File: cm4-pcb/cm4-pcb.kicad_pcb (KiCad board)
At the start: 2 copper layers, 140 x 70.5 mm, 40 parts, among them J1 Conn_01x02_Pin, J2 Conn_01x02_Pin, J3 USB1125-GF-B, J4 Conn_02x03_Odd_Even, J5 Conn_01x04, J6 Conn_01x04, J7 Conn_01x02, U1 Pfostenstecker_6_2x3, U2 Pfostenstecker_6_2x3, U3 TPD4EUSB30, U4 MagJack-A70-112-331N126, U5 SMD-PUSH-BTN, U6 TPD4EUSB30, U7 TPD4EUSB30

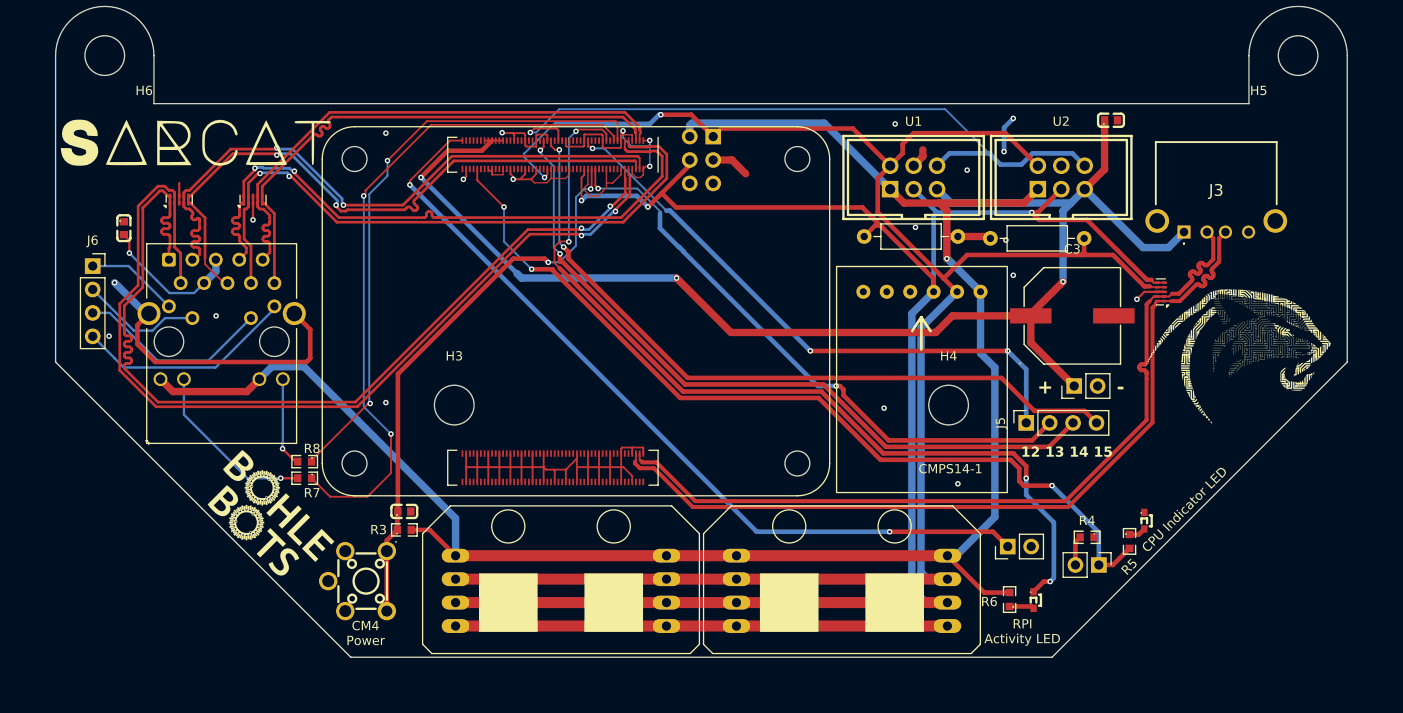
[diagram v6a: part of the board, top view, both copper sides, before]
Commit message: Smaller Footprint
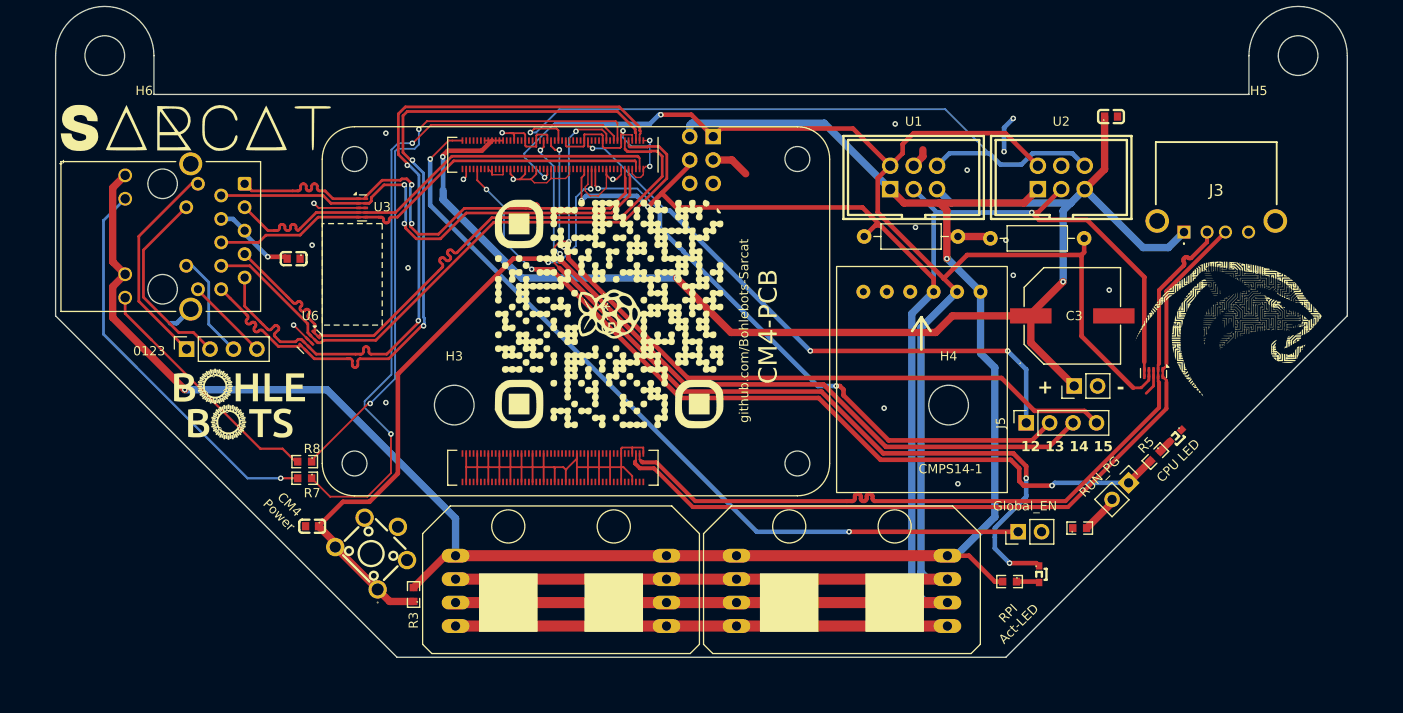
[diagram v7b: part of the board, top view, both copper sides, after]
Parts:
- added G***: LOGO, sarcat:sarcatGithub-QR, F.Cu at (-10.0, 54.8)
- moved U3 19.8 mm to (-36.8, 43.3), turned to 0 degrees
- moved C1 18.7 mm to (-44.2, 48.8), turned to 180 degrees
- moved U6 16.5 mm to (-42.5, 57.7), turned to -45 degrees
- moved J6 13.6 mm to (-55.8, 58.6), turned to 90 degrees
- moved U4 13.1 mm to (-58.4, 46.4), turned to -90 degrees
- moved G*** 12.6 mm to (-50.2, 64.6), turned to 0 degrees
- moved C2 10.1 mm to (-42.2, 77.8), turned to 180 degrees
- moved RUN_LED1 9.81 mm to (51.4, 68.0), turned to -135 degrees
- moved R5 9.66 mm to (49.2, 70.2), turned to -135 degrees
- moved J2 9.47 mm to (46.3, 73.1), turned to -45 degrees
- moved U7 8.83 mm to (49.0, 61.2), turned to -90 degrees
- moved R3 7.07 mm to (-31.2, 85.2), turned to 90 degrees
- moved U5 4.22 mm to (-35.1, 80.1), turned to 135 degrees
- moved G*** 3.16 mm to (57.4, 56.2)
- moved ACT_LED1 2.86 mm to (36.6, 83.0)
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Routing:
- net /TRD0_N: track 103.4 -> 55.8 mm
- net /TRD0_P: track 103.2 -> 55.7 mm
- net GND: track 231.0 -> 203.4 mm, vias 22 -> 23
- net Net-(U4-LEDG_K): track 19.0 -> 43.2 mm
- net /TRD3_P: track 58.1 -> 81.0 mm, vias 0 -> 2
- net /TRD3_N: track 58.1 -> 81.0 mm, vias 0 -> 2
- net +3.3V: track 203.7 -> 225.3 mm, vias 1 -> 2
- net /TRD1_N: track 69.6 -> 50.2 mm, vias 2 -> 0
- net /TRD1_P: track 69.6 -> 50.2 mm, vias 2 -> 0
- net Net-(U4-LEDY_K): track 9.78 -> 27.1 mm, vias 1 -> 0
- net /TR3_TAP: track 24.0 -> 9.13 mm
- net /TR0_TAP: track 10.1 -> 23.1 mm
- net /TR2_TAP: track 21.2 -> 11.5 mm
- net SDA: track 203.1 -> 212.6 mm
- net SHUTDOWN: track 61.0 -> 70.5 mm
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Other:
- outline, holes or cut-outs redrawn
- board text added: "0123"
- board text added: "CM4-PCB"
- board text added: "CPU LED"
- board text added: "Global_EN"
- board text added: "RPI Act-LED"
- board text added: "RUN_PG"
- board text added: "github.com/Bohlebots-Sarcat"
- board text removed: "CPU Indicator LED"
- board text removed: "RPI Activity LED"
